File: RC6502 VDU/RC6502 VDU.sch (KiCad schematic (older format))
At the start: 29 parts

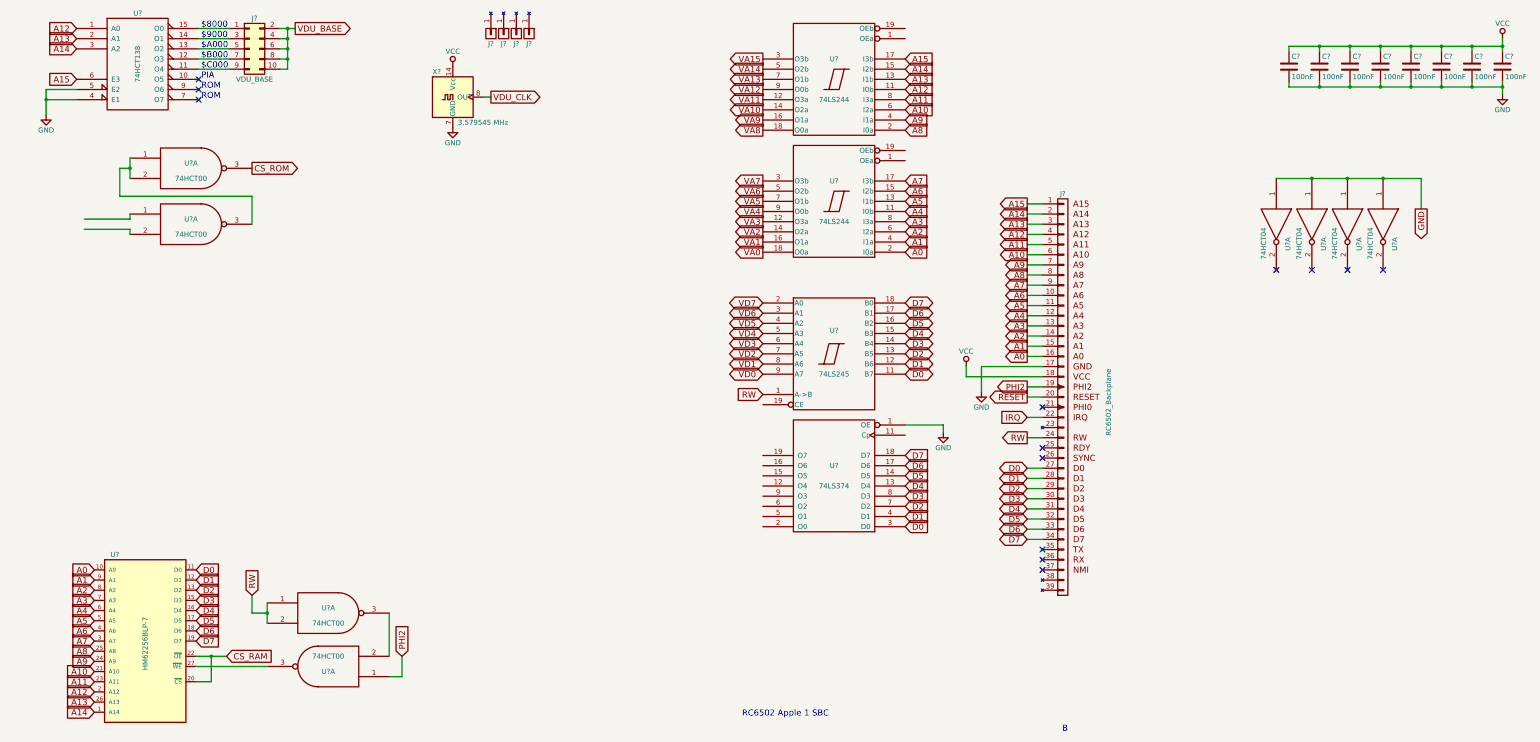
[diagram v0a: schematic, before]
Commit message: Digital logic added to schematic
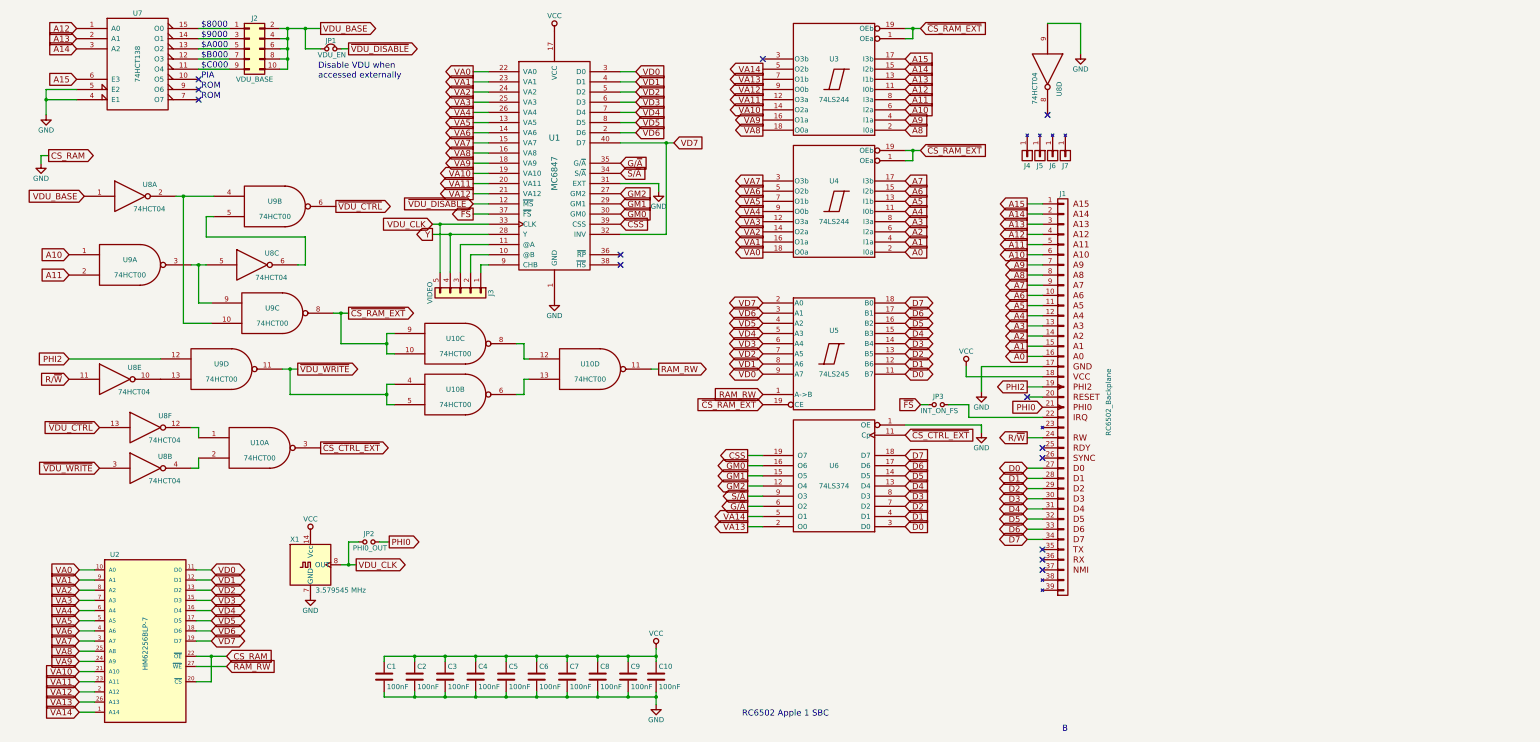
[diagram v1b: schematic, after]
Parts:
- removed U? (x4): 74HCT00, Housings_DIP:DIP-14_W7.62mm_Socket, symbol 74HCT00
- added C10, C9: 100nF, Capacitors_THT:C_Disc_D4.7mm_W2.5mm_P5.00mm, symbol C
- added J3: VIDEO, symbol Conn_01x05
- added JP1: VDU_EN, symbol Jumper_NC_Small
- added JP2: PHI0_OUT, symbol Jumper_NO_Small
- added JP3: INT_ON_FS, symbol Jumper_NO_Small
- added U1: MC6847, symbol MC6847
- added U10, U9: 74HCT00, symbol 74HCT00
- added unit 2 of U8
- added unit 4 of U8
- gave numbers to parts that had none: 22
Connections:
- net CS_RAM is gone; now on net GND: U2.20 (~CS), U2.22 (~OE)
- net A0: no longer U2.10 (A0)
- net A1: no longer U2.9 (A1)
- net A10: now also U9.1; no longer U2.21 (A10)
- net A11: now also U9.2; no longer U2.23 (A11)
- net A12: no longer U2.2 (A12)
- net A13: no longer U2.26 (A13)
- net A14: no longer U2.1 (A14)
- net A2: no longer U2.8 (A2)
- net A3: no longer U2.7 (A3)
- net A4: no longer U2.6 (A4)
- net A5: no longer U2.5 (A5)
- net A6: no longer U2.4 (A6)
- net A7: no longer U2.3 (A7)
- net A8: no longer U2.25 (A8)
- net A9: no longer U2.24 (A9)
- net D0: no longer U2.11 (D0)
- net D1: no longer U2.12 (D1)
- net D2: no longer U2.13 (D2)
- net D3: no longer U2.15 (D3)
- net D4: no longer U2.16 (D4)
- net D5: no longer U2.17 (D5)
- net D6: no longer U2.18 (D6)
- net D7: no longer U2.19 (D7)
- net GND: now also C10.2, C9.2, U1.1 (GND), U1.31 (EXT), U10.7 (GND), U10.7 (GND), U10.7 (GND), U10.7 (GND), U8.7 (GND), U8.7 (GND), U8.9, U9.7 (GND), U9.7 (GND), U9.7 (GND), U9.7 (GND); no longer U8.1, U8.1, U8.1, U8.1
- net PHI2: now also U9.12
- net VA0: now also U2.10 (A0), U1.22 (VA0)
- net VA1: now also U2.9 (A1), U1.23 (VA1)
- net VA10: now also U2.21 (A10), U1.19 (VA10)
- net VA11: now also U2.23 (A11), U1.20 (VA11)
- net VA12: now also U2.2 (A12), U1.21 (VA12)
- net VA13: now also U2.26 (A13), U6.2 (O0)
- net VA14: now also U2.1 (A14), U6.5 (O1)
- net VA2: now also U2.8 (A2), U1.24 (VA2)
- net VA3: now also U2.7 (A3), U1.25 (VA3)
- net VA4: now also U2.6 (A4), U1.26 (VA4)
- net VA5: now also U2.5 (A5), U1.13 (VA5)
- net VA6: now also U2.4 (A6), U1.14 (VA6)
- net VA7: now also U2.3 (A7), U1.15 (VA7)
- net VA8: now also U2.25 (A8), U1.16 (VA8)
- net VA9: now also U2.24 (A9), U1.18 (VA9)
- net VCC: now also C10.1, C9.1, U1.17 (VCC), U10.14 (VCC), U10.14 (VCC), U10.14 (VCC), U10.14 (VCC), U8.14 (VCC), U8.14 (VCC), U9.14 (VCC), U9.14 (VCC), U9.14 (VCC), U9.14 (VCC)
- net VD0: now also U2.11 (D0), U1.3 (D0)
- net VD1: now also U2.12 (D1), U1.4 (D1)
- net VD2: now also U2.13 (D2), U1.5 (D2)
- net VD3: now also U2.15 (D3), U1.6 (D3)
- net VD4: now also U2.16 (D4), U1.7 (D4)
- net VD5: now also U2.17 (D5), U1.8 (D5)
- net VD6: now also U2.18 (D6), U1.2 (D6)
- net VD7: now also U2.19 (D7), U1.32 (INV), U1.40 (D7)
- net VDU_BASE: now also U8.1, JP1.1
- net VDU_CLK: now also J3.5 (Pin_5), JP2.1, U1.33 (CLK)
- net RAM_RW: now reaches U2.27 (~WE)
- net RAM_RW: now also U5.1 (A->B), U10.11
- net at U8.2: now also U9.10, U9.4
- net PHI0: now reaches J1.21 (PHI0)
- net PHI0: now also JP2.2
- net ~CS_CTRL_EXT: now reaches U6.11 (Cp)
- net ~CS_CTRL_EXT: now also U10.3
- net GM2: now reaches U6.12 (O4)
- net GM2: now also U1.27 (GM2)
- net GM1: now reaches U6.15 (O5)
- net GM1: now also U1.29 (GM1)
- net GM0: now reaches U6.16 (O6)
- net GM0: now also U1.30 (GM0)
- net CSS: now reaches U6.19 (O7)
- net CSS: now also U1.39 (CSS)
- net G/~A: now reaches U6.6 (O2)
- net G/~A: now also U1.35 (G/~A)
- net S/~A: now reaches U6.9 (O3)
- net S/~A: now also U1.34 (S/~A)
- net ~CS_RAM_EXT: now reaches U4.1 (OEa)
- net ~CS_RAM_EXT: now also U3.1 (OEa), U3.19 (OEb), U4.19 (OEb), U5.19 (CE), U10.10, U10.9, U9.8
- net IRQ: no longer names the net of J1.22 (IRQ)
- net IRQ: now also JP3.2
- net RESET: no longer names the net of J1.20 (RESET)
- net RW renamed R/~W
- net R/~W: now also U8.11; no longer U5.1 (A->B)
- net VA15: no longer names the net of U3.3 (O3b)
- new net: U10.1, U8.12
- new net: U8.10, U9.13
- new net: U8.5, U9.3, U9.9
- new net: U8.6, U9.5
- new net: J3.2 (Pin_2), U1.10 (@B)
- new net: J3.3 (Pin_3), U1.11 (@A)
- new net: J3.1 (Pin_1), U1.9 (CHB)
- new net: U10.2, U8.4
- new net: U10.13, U10.6
- new net: U10.12, U10.8
- new net Y: J3.4 (Pin_4), U1.28 (Y)
- new net ~FS: JP3.1, U1.37 (~FS)
- new net ~VDU_CTRL: U8.13, U9.6
- new net ~VDU_DISABLE: JP1.2, U1.12 (~MS)
- new net ~VDU_WRITE: U10.4, U10.5, U8.3, U9.11
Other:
- note added: "Disable VDU when\naccessed externally"
- moved on the sheet: C1, C2, C3, C4, C5, C6, C7, C8, J4, J5, J6, J7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

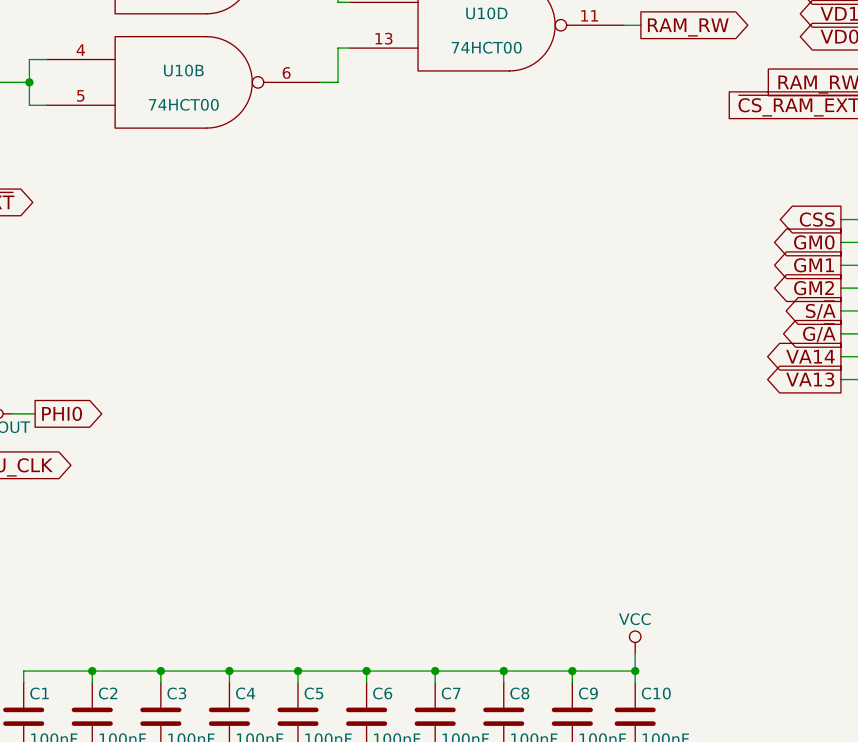
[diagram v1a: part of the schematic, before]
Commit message: Added analog circuit
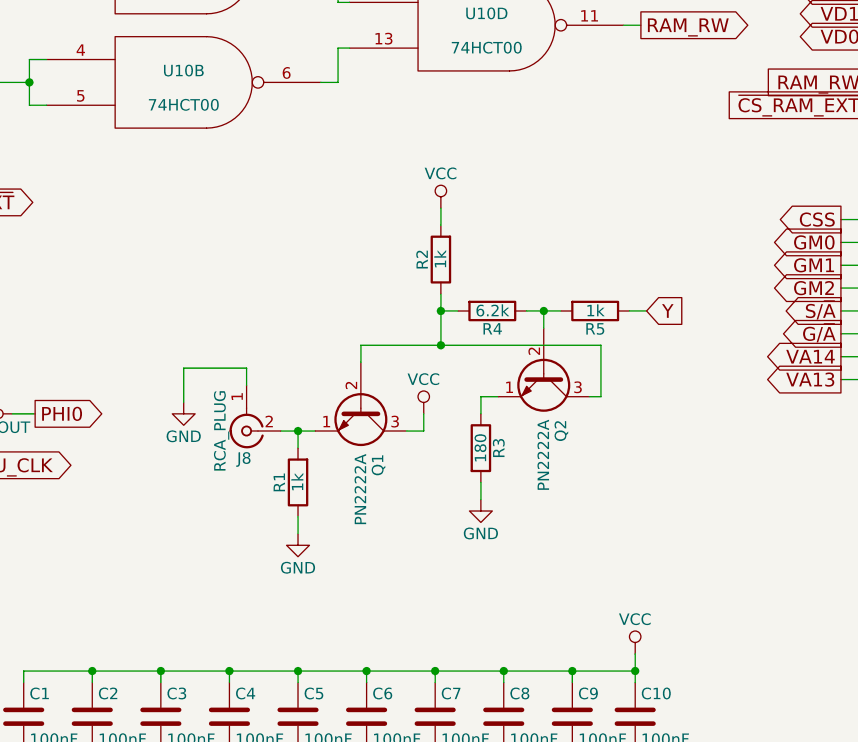
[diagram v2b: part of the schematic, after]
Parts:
- added J8: RCA_PLUG, symbol RCA_PLUG
- added Q1, Q2: PN2222A, TO_SOT_Packages_THT:TO-92_Molded_Narrow, symbol PN2222A
- added R1, R2, R5: 1k, symbol R
- added R3: 180, symbol R
- added R4: 6.2k, symbol R
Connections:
- net GND: now also J8.1 (Ext), R1.1, R3.2
- net VCC: now also Q1.3 (C), R2.2
- net Y: now also R5.1
- new net: Q2.1 (E), R3.1
- new net: Q2.2 (B), R4.1, R5.2
- new net: Q1.2 (B), Q2.3 (C), R2.1, R4.2
- new net: J8.2 (In), Q1.1 (E), R1.2
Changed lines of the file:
@@
 LIBS:oscillator
 LIBS:mc6847
+LIBS:rca_plug
 LIBS:RC6502 VDU-cache
 EELAYER 25 0
@@
 Text GLabel 4400 2750 0    60   Output ~ 0
 Y
+$Comp
+L PN2222A Q2
+U 1 1 5C0D8044
+P 6200 5600
+F 0 "Q2" H 6400 5675 50  0000 L CNN
+F 1 "PN2222A" H 6400 5600 50  0000 L CNN
+F 2 "TO_SOT_Packages_THT:TO-92_Molded_Narrow" H 6400 5525 50  0001 L CIN
+F 3 "" H 6200 5600 50  0001 L CNN
+	1    6200 5600
+	0    1    1    0
+$EndComp
+$Comp
+L PN2222A Q1
+U 1 1 5C0D851A
+P 5400 5750
+F 0 "Q1" H 5600 5825 50  0000 L CNN
+F 1 "PN2222A" H 5600 5750 50  0000 L CNN
+F 2 "TO_SOT_Packages_THT:TO-92_Molded_Narrow" H 5600 5675 50  0001 L CIN
+F 3 "" H 5400 5750 50  0001 L CNN
+	1    5400 5750
+	0    1    1    0
+$EndComp
+Text GLabel 6650 5325 2    60   Input ~ 0
+Y
+$Comp
+L R R5
+U 1 1 5C0D8B35
+P 6425 5325
+F 0 "R5" V 6505 5325 50  0000 C CNN
+F 1 "1k" V 6425 5325 50  0000 C CNN
+F 2 "" V 6355 5325 50  0001 C CNN
+F 3 "" H 6425 5325 50  0001 C CNN
+	1    6425 5325
+	0    1    1    0
+$EndComp
+Wire Wire Line
+	6575 5325 6650 5325
+Wire Wire Line
+	6125 5325 6275 5325
+Wire Wire Line
+	6200 5325 6200 5400
+Wire Wire Line
+	6000 5700 5925 5700
+Wire Wire Line
+	5925 5700 5925 5775
+$Comp
+L R R3
+U 1 1 5C0D9C99
+P 5925 5925
+F 0 "R3" V 6005 5925 50  0000 C CNN
+F 1 "180" V 5925 5925 50  0000 C CNN
+F 2 "" V 5855 5925 50  0001 C CNN
+F 3 "" H 5925 5925 50  0001 C CNN
+	1    5925 5925
+	1    0    0    -1
+$EndComp
+$Comp
+L GND #PWR014
+U 1 1 5C0DA1BF
+P 5925 6150
+F 0 "#PWR014" H 5925 5900 50  0001 C CNN
+F 1 "GND" H 5925 6000 50  0000 C CNN
+F 2 "" H 5925 6150 50  0001 C CNN
+F 3 "" H 5925 6150 50  0001 C CNN
+	1    5925 6150
+	1    0    0    -1
+$EndComp
+Wire Wire Line
+	5925 6150 5925 6075
+$Comp
+L R R4
+U 1 1 5C0DAB87
+P 5975 5325
+F 0 "R4" V 6055 5325 50  0000 C CNN
+F 1 "6.2k" V 5975 5325 50  0000 C CNN
+F 2 "" V 5905 5325 50  0001 C CNN
+F 3 "" H 5975 5325 50  0001 C CNN
+	1    5975 5325
+	0    1    1    0
+$EndComp
+$Comp
+L R R2
+U 1 1 5C0DACBD
+P 5750 5100
+F 0 "R2" V 5830 5100 50  0000 C CNN
+F 1 "1k" V 5750 5100 50  0000 C CNN
+F 2 "" V 5680 5100 50  0001 C CNN
+F 3 "" H 5750 5100 50  0001 C CNN
+	1    5750 5100
+	-1   0    0    1
+$EndComp
+Connection ~ 6200 5325
+$Comp
+L VCC #PWR015
+U 1 1 5C0DBAFF
+P 5750 4875
+F 0 "#PWR015" H 5750 4725 50  0001 C CNN
+F 1 "VCC" H 5750 5025 50  0000 C CNN
+F 2 "" H 5750 4875 50  0001 C CNN
+F 3 "" H 5750 4875 50  0001 C CNN
+	1    5750 4875
+	1    0    0    -1
+$EndComp
+Wire Wire Line
+	5750 4875 5750 4950
+Wire Wire Line
+	6400 5700 6450 5700
+Wire Wire Line
+	6450 5700 6450 5475
+Wire Wire Line
+	6450 5475 5400 5475
+Wire Wire Line
+	5750 5250 5750 5475
+Wire Wire Line
+	5750 5325 5825 5325
+Connection ~ 5750 5325
+Wire Wire Line
+	5400 5475 5400 5550
+Connection ~ 5750 5475
+$Comp
+L VCC #PWR016
+U 1 1 5C0DD54D
+P 5675 5775
+F 0 "#PWR016" H 5675 5625 50  0001 C CNN
+F 1 "VCC" H 5675 5925 50  0000 C CNN
+F 2 "" H 5675 5775 50  0001 C CNN
+F 3 "" H 5675 5775 50  0001 C CNN
+	1    5675 5775
+	1    0    0    -1
+$EndComp
+Wire Wire Line
+	5600 5850 5675 5850
+Wire Wire Line
+	5675 5850 5675 5775
+$Comp
+L R R1
+U 1 1 5C0DDB64
+P 5125 6075
+F 0 "R1" V 5205 6075 50  0000 C CNN
+F 1 "1k" V 5125 6075 50  0000 C CNN
+F 2 "" V 5055 6075 50  0001 C CNN
+F 3 "" H 5125 6075 50  0001 C CNN
+	1    5125 6075
+	-1   0    0    1
+$EndComp
+Wire Wire Line
+	5125 5925 5125 5850
+Wire Wire Line
+	5050 5850 5200 5850
+Wire Wire Line
+	5125 6225 5125 6300
+$Comp
+L GND #PWR017
+U 1 1 5C0DE051
+P 5125 6300
+F 0 "#PWR017" H 5125 6050 50  0001 C CNN
+F 1 "GND" H 5125 6150 50  0000 C CNN
+F 2 "" H 5125 6300 50  0001 C CNN
+F 3 "" H 5125 6300 50  0001 C CNN
+	1    5125 6300
+	1    0    0    -1
+$EndComp
+$Comp
+L RCA_PLUG J8
+U 1 1 5C0DE558
+P 4900 5850
+F 0 "J8" H 4910 5970 50  0000 C CNN
+F 1 "RCA_PLUG" V 5015 5850 50  0000 C CNN
+F 2 "" H 4900 5850 50  0001 C CNN
+F 3 "" H 4900 5850 50  0001 C CNN
+	1    4900 5850
+	-1   0    0    1
+$EndComp
+Connection ~ 5125 5850
+$Comp
+L GND #PWR018
+U 1 1 5C0DF101
+P 4625 5725
+F 0 "#PWR018" H 4625 5475 50  0001 C CNN
+F 1 "GND" H 4625 5575 50  0000 C CNN
+F 2 "" H 4625 5725 50  0001 C CNN
+F 3 "" H 4625 5725 50  0001 C CNN
+	1    4625 5725
+	1    0    0    -1
+$EndComp
+Wire Wire Line
+	4625 5725 4625 5575
+Wire Wire Line
+	4625 5575 4900 5575
+Wire Wire Line
+	4900 5575 4900 5650
 $EndSCHEMATC

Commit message: Added description
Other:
- note added: "A"
- note added: "Display adapter based on the Motorola 6847 Video Display Generator (VDG), this maps\ninto the memory space and does not follow the designs of the Apple 1 computer,\ninstead it is only intended for use with the RC6502 computer."
- note removed: "B"
- moved on the sheet: U6
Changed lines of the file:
@@
 RC6502 Apple 1 SBC
 Text Notes 10650 7650 2    60   ~ 0
-B
+A
 $Comp
 L 74LS138 U7
@@
 L 74LS374 U6
 U 1 1 5C049977
-P 8350 5125
-F 0 "U6" H 8350 5025 50  0000 C CNN
-F 1 "74LS374" H 8350 5225 50  0000 C CNN
-F 2 "" H 8350 5125 50  0001 C CNN
-F 3 "" H 8350 5125 50  0001 C CNN
-	1    8350 5125
+P 8350 5400
+F 0 "U6" H 8350 5300 50  0000 C CNN
+F 1 "74LS374" H 8350 5500 50  0000 C CNN
+F 2 "" H 8350 5400 50  0001 C CNN
+F 3 "" H 8350 5400 50  0001 C CNN
+	1    8350 5400
 	-1   0    0    1
 $EndComp
-Text GLabel 9050 4925 2    60   Input ~ 0
+Text GLabel 9050 5200 2    60   Input ~ 0
 D7
-Text GLabel 9050 5025 2    60   Input ~ 0
+Text GLabel 9050 5300 2    60   Input ~ 0
 D6
-Text GLabel 9050 5125 2    60   Input ~ 0
+Text GLabel 9050 5400 2    60   Input ~ 0
 D5
-Text GLabel 9050 5225 2    60   Input ~ 0
+Text GLabel 9050 5500 2    60   Input ~ 0
 D4
-Text GLabel 9050 5325 2    60   Input ~ 0
+Text GLabel 9050 5600 2    60   Input ~ 0
 D3
-Text GLabel 9050 5425 2    60   Input ~ 0
+Text GLabel 9050 5700 2    60   Input ~ 0
 D2
-Text GLabel 9050 5525 2    60   Input ~ 0
+Text GLabel 9050 5800 2    60   Input ~ 0
 D1
-Text GLabel 9050 5625 2    60   Input ~ 0
+Text GLabel 9050 5900 2    60   Input ~ 0
 D0
 $Comp
@@
 L GND #PWR08
 U 1 1 5C04E709
-P 9800 4700
-F 0 "#PWR08" H 9800 4450 50  0001 C CNN
-F 1 "GND" H 9800 4550 50  0000 C CNN
-F 2 "" H 9800 4700 50  0001 C CNN
-F 3 "" H 9800 4700 50  0001 C CNN
-	1    9800 4700
-	1    0    0    -1
-$EndComp
-Wire Wire Line
-	9050 4625 9800 4625
+P 9800 4975
+F 0 "#PWR08" H 9800 4725 50  0001 C CNN
+F 1 "GND" H 9800 4825 50  0000 C CNN
+F 2 "" H 9800 4975 50  0001 C CNN
+F 3 "" H 9800 4975 50  0001 C CNN
+	1    9800 4975
+	1    0    0    -1
+$EndComp
+Wire Wire Line
+	9050 4900 9800 4900
 Text GLabel 7650 3425 0    60   BiDi ~ 0
 VD7
@@
 Text GLabel 925  6850 0    60   Input ~ 0
 VA8
-Text GLabel 7500 5525 0    60   Output ~ 0
+Text GLabel 7500 5800 0    60   Output ~ 0
 VA14
-Text GLabel 7500 5625 0    60   Output ~ 0
+Text GLabel 7500 5900 0    60   Output ~ 0
 VA13
 Text GLabel 925  7450 0    60   Input ~ 0
@@
 NoConn ~ 6250 2950
 Wire Wire Line
-	7500 5525 7650 5525
-Wire Wire Line
-	7500 5625 7650 5625
+	7500 5800 7650 5800
+Wire Wire Line
+	7500 5900 7650 5900
 Text GLabel 10400 4450 0    60   Input ~ 0
 PHI0
@@
 Text GLabel 6250 2050 2    60   Input ~ 0
 G/~A
-Text GLabel 7500 5425 0    60   Output ~ 0
+Text GLabel 7500 5700 0    60   Output ~ 0
 G/~A
 Text GLabel 6250 2150 2    60   Input ~ 0
 S/~A
-Text GLabel 7500 5325 0    60   Output ~ 0
+Text GLabel 7500 5600 0    60   Output ~ 0
 S/~A
 Text GLabel 6250 2350 2    60   Input ~ 0
@@
 Text GLabel 6250 2650 2    60   Input ~ 0
 CSS
-Text GLabel 7500 4925 0    60   Output ~ 0
+Text GLabel 7500 5200 0    60   Output ~ 0
 CSS
-Text GLabel 7500 5025 0    60   Output ~ 0
+Text GLabel 7500 5300 0    60   Output ~ 0
 GM0
-Text GLabel 7500 5125 0    60   Output ~ 0
+Text GLabel 7500 5400 0    60   Output ~ 0
 GM1
-Text GLabel 7500 5225 0    60   Output ~ 0
+Text GLabel 7500 5500 0    60   Output ~ 0
 GM2
 Wire Wire Line
-	7500 4925 7650 4925
-Wire Wire Line
-	7650 5025 7500 5025
-Wire Wire Line
-	7500 5125 7650 5125
-Wire Wire Line
-	7650 5225 7500 5225
-Wire Wire Line
-	7500 5325 7650 5325
-Wire Wire Line
-	7650 5425 7500 5425
+	7500 5200 7650 5200
+Wire Wire Line
+	7650 5300 7500 5300
+Wire Wire Line
+	7500 5400 7650 5400
+Wire Wire Line
+	7650 5500 7500 5500
+Wire Wire Line
+	7500 5600 7650 5600
+Wire Wire Line
+	7650 5700 7500 5700
 $Comp
 L GND #PWR010
@@
 Wire Wire Line
 	3500 925  3575 925
-Text GLabel 9050 4725 2    60   Input ~ 0
+Text GLabel 9050 5000 2    60   Input ~ 0
 ~CS_CTRL_EXT
 Text GLabel 9200 725  2    60   Input ~ 0
@@
 ~VDU_WRITE
 Wire Wire Line
-	9800 4625 9800 4700
+	9800 4900 9800 4975
 Wire Wire Line
 	2025 5050 2100 5050
@@
 Wire Wire Line
 	4900 5575 4900 5650
+Text Notes 7025 6875 0    60   ~ 0
+Display adapter based on the Motorola 6847 Video Display Generator (VDG), this maps\ninto the memory space and does not follow the designs of the Apple 1 computer,\ninstead it is only intended for use with the RC6502 computer.
 $EndSCHEMATC
